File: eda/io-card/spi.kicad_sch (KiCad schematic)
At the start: 12 parts, among them U11 74HCT193, U16 74HCT138, U17 74HCT574, U18 74HCT74, U19 74HCT157, U20 74HCT595, U21 74HCT165, U22 74HCT193, X1 ? Mhz

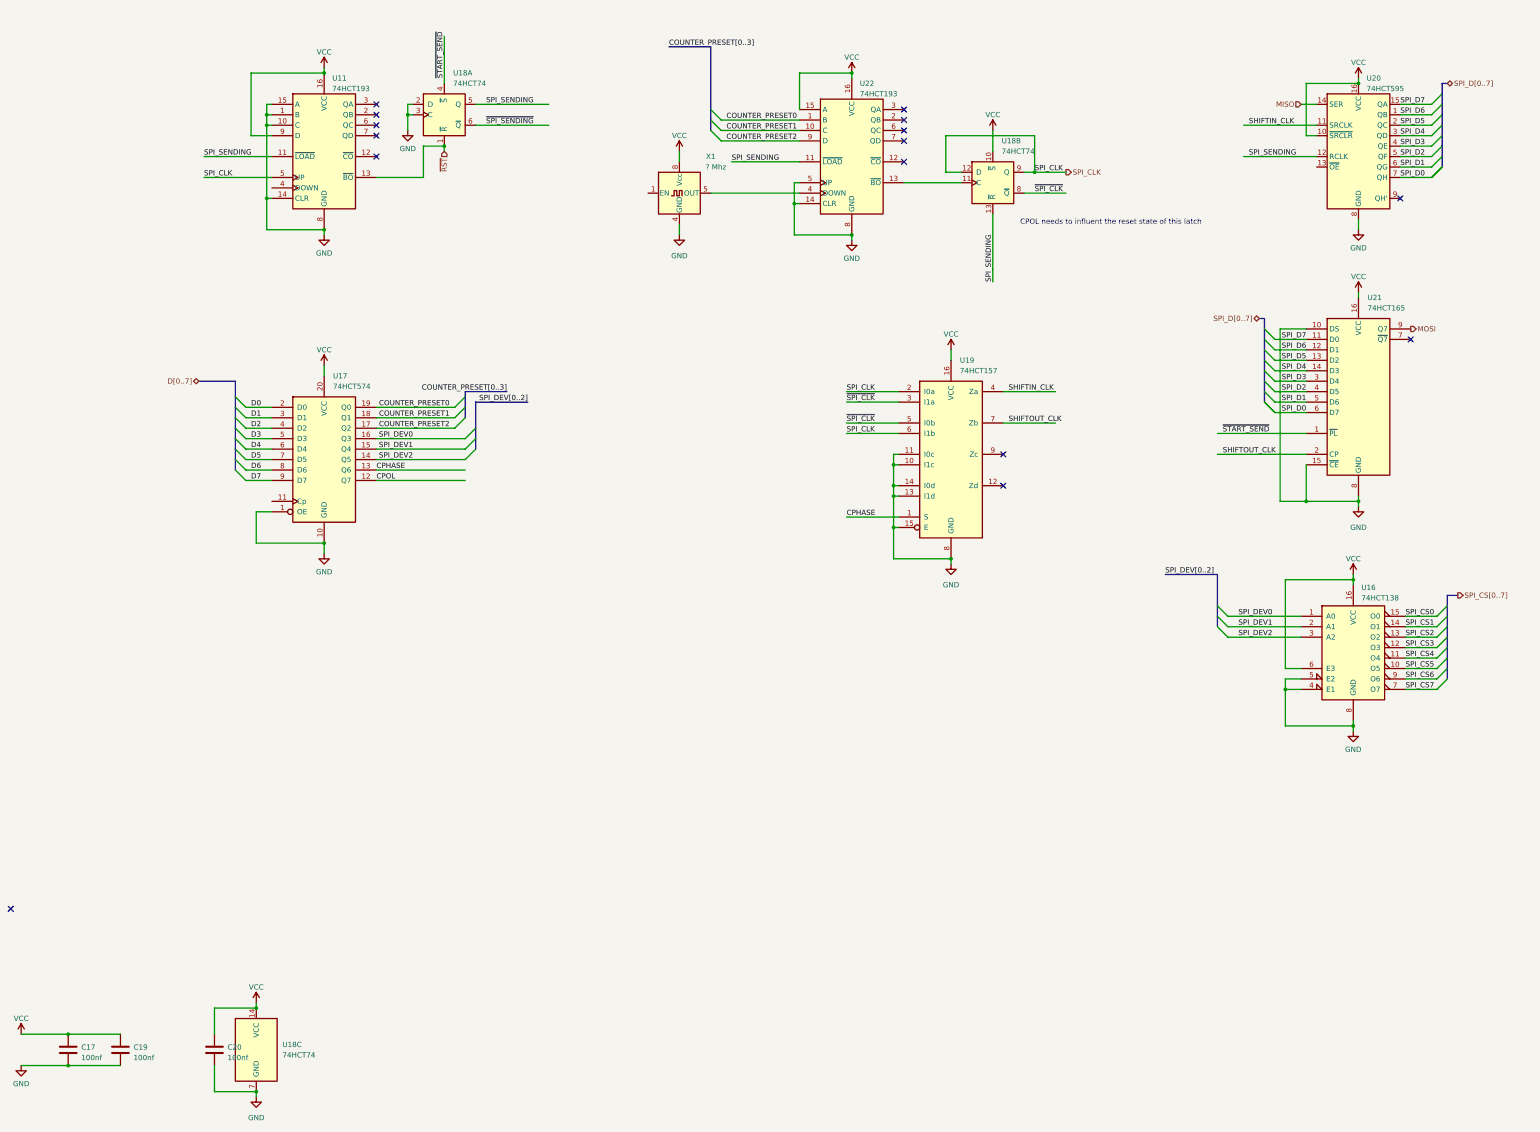
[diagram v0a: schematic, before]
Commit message: Add address decode
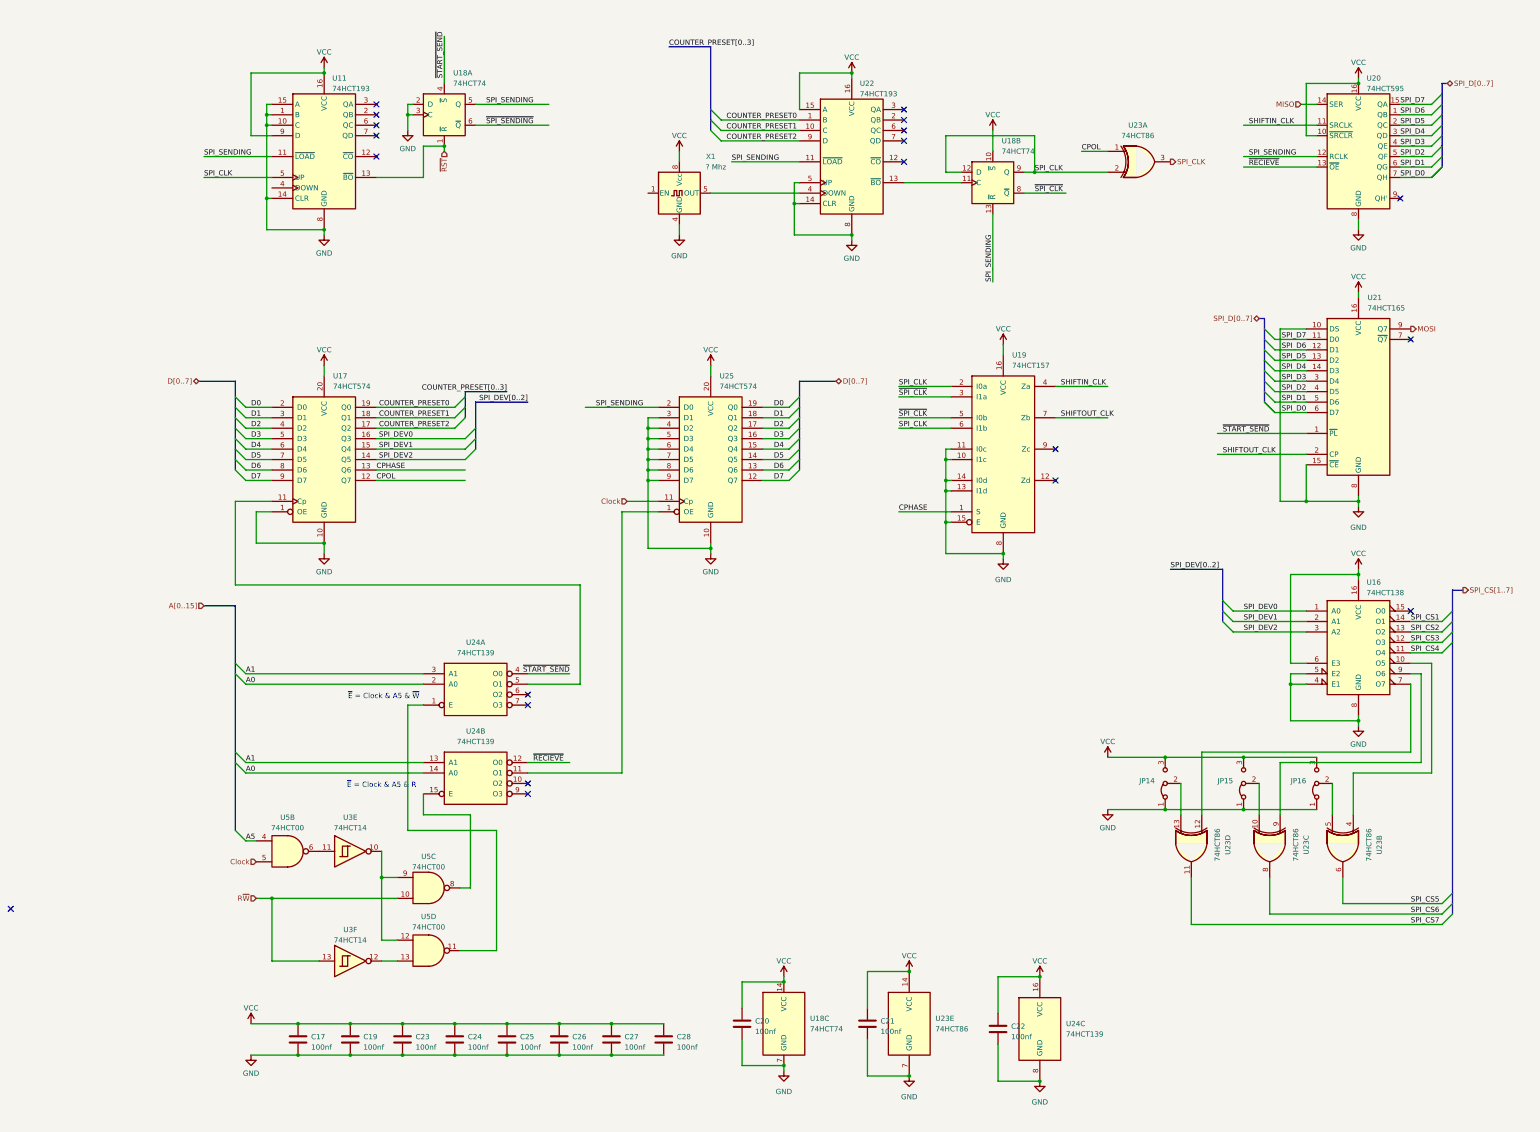
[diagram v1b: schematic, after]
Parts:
- added C21, C22, C23, C24, C25, C26, C27, C28: 100nf, Capacitor_THT:C_Disc_D3.8mm_W2.6mm_P2.50mm, symbol Device:C
- added JP14, JP15, JP16: ~, symbol Jumper:Jumper_3_Bridged12
- added U23: 74HCT86, symbol 74xx:74LS86
- added U24: 74HCT139, symbol 74xx:74LS139
- added U25: 74HCT574, symbol 74xx:74HCT574
- added U3: 74HCT14, Package_DIP:DIP-14_W7.62mm, symbol 74xx:74LS14
- added U5: 74HCT00, Package_DIP:DIP-14_W7.62mm, symbol 74xx:74HCT00
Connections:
- net CPOL: now also U23.1
- net D0: now also U25.19 (Q0)
- net D1: now also U25.18 (Q1)
- net D2: now also U25.17 (Q2)
- net D3: now also U25.16 (Q3)
- net D4: now also U25.15 (Q4)
- net D5: now also U25.14 (Q5)
- net D6: now also U25.13 (Q6)
- net D7: now also U25.12 (Q7)
- net GND: now also C21.2, C22.2, C23.2, C24.2, C25.2, C26.2, C27.2, C28.2, JP14.1 (A), JP15.1 (A), JP16.1 (A), U23.7 (GND), U24.8 (GND), U25.10 (GND), U25.3 (D1), U25.4 (D2), U25.5 (D3), U25.6 (D4), U25.7 (D5), U25.8 (D6), U25.9 (D7)
- net SPI_CLK: now also U23.2, U23.3
- net SPI_CS5: now also U23.6; no longer U16.10 (O5)
- net SPI_CS6: now also U23.8; no longer U16.9 (O6)
- net SPI_CS7: now also U23.11; no longer U16.7 (O7)
- net SPI_SENDING: now also U25.2 (D0)
- net VCC: now also C21.1, C22.1, C23.1, C24.1, C25.1, C26.1, C27.1, C28.1, JP14.3 (B), JP15.3 (B), JP16.3 (B), U23.14 (VCC), U24.16 (VCC), U25.20 (VCC)
- net ~{START_SEND}: now also U24.4 (O0)
- net at U17.11 (Cp): now also U24.5 (O1)
- net ~{RECIEVE}: now reaches U20.13 (~{OE})
- net ~{RECIEVE}: now also U24.12 (O0)
- net SPI_CS0: no longer names the net of U16.15 (O0)
- new net: U24.11 (O1), U25.1 (OE)
- new net: U24.15 (E), U5.8
- new net: U3.12, U5.13
- new net: JP16.2 (C), U23.5
- new net: JP14.2 (C), U23.13
- new net: U3.10, U5.12, U5.9
- new net: U3.11, U5.6
- new net: U24.1 (E), U5.11
- new net: U16.10 (O5), U23.4
- new net: JP15.2 (C), U23.10
- new net: U16.7 (O7), U23.12
- new net: U16.9 (O6), U23.9
- new net A0: U24.14 (A0), U24.2 (A0)
- new net A1: U24.13 (A1), U24.3 (A1)
- new net A5: U5.4
- new net Clock: U25.11 (Cp), U5.5
- new net R~{W}: U3.13, U5.10
- no-connect marks 15 -> 20
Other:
- note added: "~{E} = Clock & A5 & R"
- note added: "~{E} = Clock & A5 & ~{W}"
- note removed: "CPOL needs to influent the reset state of this latch"
- moved on the sheet: C17, C19, C20, U16, U18C, U19

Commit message: Add memcontrol display to panels
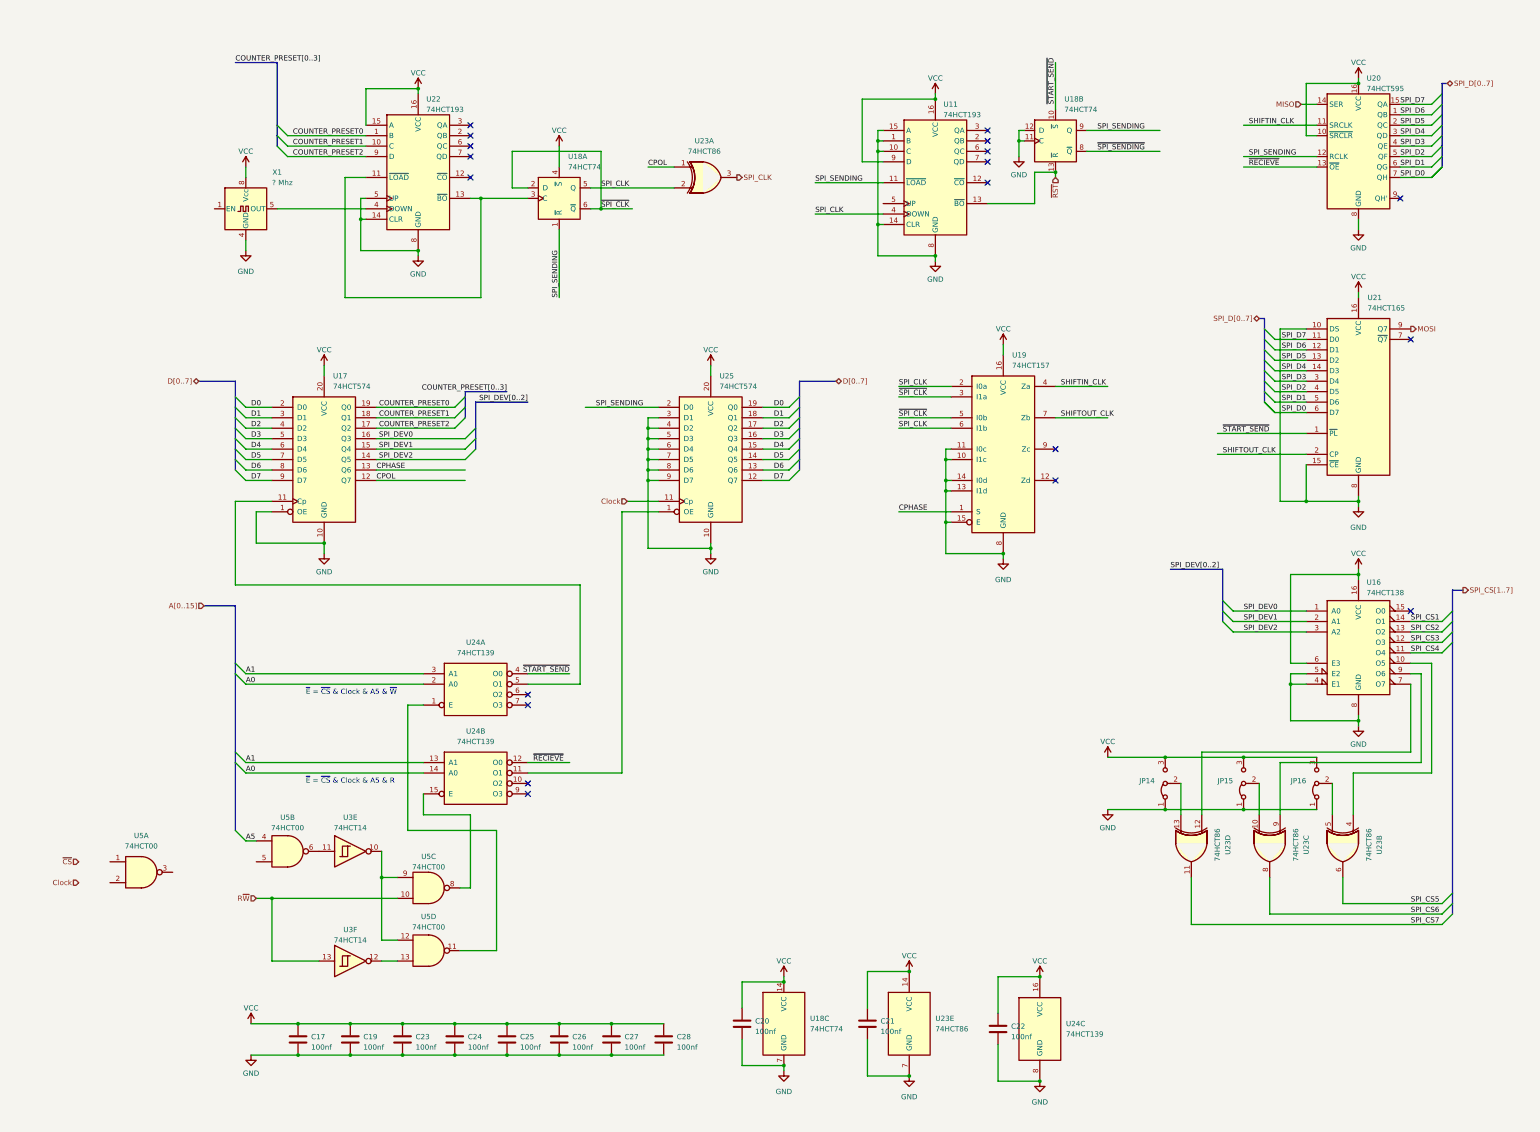
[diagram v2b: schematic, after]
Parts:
- added unit 1 of U5
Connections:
- net Clock: no longer U5.5
- net GND: now also U18.11 (C), U18.12 (D); no longer U18.2 (D), U18.3 (C)
- net SPI_CLK: now also U11.4 (DOWN), U18.2 (D), U18.5 (Q), U18.6 (~{Q}), U19.3 (I1a), U19.5 (I0b); no longer U11.5 (UP), U18.12 (D), U18.9 (Q)
- net SPI_SENDING: now also U18.1 (~{R}), U18.9 (Q); no longer U18.13 (~{R}), U18.5 (Q), U22.11 (~{LOAD})
- net VCC: now also U18.4 (~{S}); no longer U18.10 (~{S})
- net ~{RST}: now also U18.13 (~{R}); no longer U18.1 (~{R})
- net ~{SPI_SENDING}: now also U18.8 (~{Q}); no longer U18.6 (~{Q})
- net ~{START_SEND}: now also U18.10 (~{S}); no longer U18.4 (~{S})
- net at U22.13 (~{BO}): now also U18.3 (C), U22.11 (~{LOAD}); no longer U18.11 (C)
- removed net ~{SPI_CLK}: U18.8 (~{Q}), U19.3 (I1a), U19.5 (I0b)
- no-connect marks 20 -> 19
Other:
- note added: "~{E} = ~{CS} & Clock & A5 & R"
- note added: "~{E} = ~{CS} & Clock & A5 & ~{W}"
- note removed: "~{E} = Clock & A5 & R"
- note removed: "~{E} = Clock & A5 & ~{W}"
- moved on the sheet: U11, U18A, U18B, U22, U23A, X1
